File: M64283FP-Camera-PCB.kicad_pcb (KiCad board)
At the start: 2 copper layers, 21.8 x 21.4 mm, 8 parts, among them J1 JST_Connector, U1 M64283FP

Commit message: Add preview image Optimize labels
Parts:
- renumbered TADD to TP1, STRB to TP2
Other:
- board text added: "STRB"
- board text added: "TADD"
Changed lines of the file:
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@@
     (descr "SMD rectangular pad as test Point, square 1.5mm side length")
     (tags "test point SMD pad rectangle square")
-    (property "Sheetfile" "GBC Sensor breakout.kicad_sch")
+    (property "Sheetfile" "M64283FP-Camera-PCB.kicad_sch")
     (property "Sheetname" "")
     (attr exclude_from_pos_files)
-    (fp_text reference "STRB" (at 0 1.4) (layer "F.SilkS")
+    (fp_text reference "TP2" (at 0 1.4) (layer "F.SilkS") hide
       (effects (font (size 0.5 0.5) (thickness 0.1)))
     )
-    (fp_text value "TestPoint" (at 0 1.75) (layer "F.Fab")
+    (fp_text value "TestPoint" (at 0 5.461) (layer "F.Fab")
       (effects (font (size 1 1) (thickness 0.15)))
     )
@@
     (descr "Capacitor SMD 0603 (1608 Metric), square (rectangular) end terminal, IPC_7351 nominal with elongated pad for handsoldering. (Body size source: IPC-SM-782 page 76, https://www.pcb-3d.com/wordpress/wp-content/uploads/ipc-sm-782a_amendment_1_and_2.pdf), generated with kicad-footprint-generator")
     (tags "capacitor handsolder")
-    (property "Sheetfile" "GBC Sensor breakout.kicad_sch")
+    (property "Sheetfile" "M64283FP-Camera-PCB.kicad_sch")
     (property "Sheetname" "")
     (attr smd)
@@
     (descr "Inductor SMD 1210 (3225 Metric), square (rectangular) end terminal, IPC_7351 nominal with elongated pad for handsoldering. (Body size source: http://www.tortai-tech.com/upload/download/2011102023233369053.pdf), generated with kicad-footprint-generator")
     (tags "inductor handsolder")
-    (property "Sheetfile" "GBC Sensor breakout.kicad_sch")
+    (property "Sheetfile" "M64283FP-Camera-PCB.kicad_sch")
     (property "Sheetname" "")
     (attr smd)
@@
     (descr "Capacitor SMD 0603 (1608 Metric), square (rectangular) end terminal, IPC_7351 nominal with elongated pad for handsoldering. (Body size source: IPC-SM-782 page 76, https://www.pcb-3d.com/wordpress/wp-content/uploads/ipc-sm-782a_amendment_1_and_2.pdf), generated with kicad-footprint-generator")
     (tags "capacitor handsolder")
-    (property "Sheetfile" "GBC Sensor breakout.kicad_sch")
+    (property "Sheetfile" "M64283FP-Camera-PCB.kicad_sch")
     (property "Sheetname" "")
     (attr smd)
@@
   (footprint "JST Connector:JST Connector" (layer "F.Cu")
     (at 130.9 93.9 180)
-    (property "Sheetfile" "GBC Sensor breakout.kicad_sch")
+    (property "Sheetfile" "M64283FP-Camera-PCB.kicad_sch")
     (property "Sheetname" "")
     (attr smd)
@@
     (descr "SMD rectangular pad as test Point, square 1.5mm side length")
     (tags "test point SMD pad rectangle square")
-    (property "Sheetfile" "GBC Sensor breakout.kicad_sch")
+    (property "Sheetfile" "M64283FP-Camera-PCB.kicad_sch")
     (property "Sheetname" "")
     (attr exclude_from_pos_files)
-    (fp_text reference "TADD" (at 0 1.4) (layer "F.SilkS")
+    (fp_text reference "TP1" (at 0 1.4) (layer "F.SilkS") hide
       (effects (font (size 0.5 0.5) (thickness 0.1)))
     )
-    (fp_text value "TestPoint" (at 0 1.75) (layer "F.Fab")
+    (fp_text value "TestPoint" (at 0 5.461) (layer "F.Fab")
       (effects (font (size 1 1) (thickness 0.15)))
     )
@@
   (footprint "M6428xFP:M6428xFP" (layer "B.Cu")
     (at 130.9 90.05 180)
-    (property "Sheetfile" "GBC Sensor breakout.kicad_sch")
+    (property "Sheetfile" "M64283FP-Camera-PCB.kicad_sch")
     (property "Sheetname" "")
     (attr smd)
@@
   (gr_line (start 140.3 94.7) (end 140.3 92.1) (layer "Edge.Cuts") (width 0.1))
   (gr_arc (start 120 82.2) (mid 120.058579 82.058579) (end 120.2 82) (layer "Edge.Cuts") (width 0.1))
+  (gr_text "TADD" (at 132.065 99.495) (layer "F.SilkS")
+    (effects (font (size 0.5 0.5) (thickness 0.1)))
+  )
+  (gr_text "STRB" (at 135.6 99.495) (layer "F.SilkS")
+    (effects (font (size 0.5 0.5) (thickness 0.1)))
+  )
   (segment (start 136.9 90.9) (end 135.9 89.9) (width 0.25) (layer "F.Cu") (net 1))
   (segment (start 126.1625 85.4555) (end 126.1625 86.384) (width 0.25) (layer "F.Cu") (net 1))

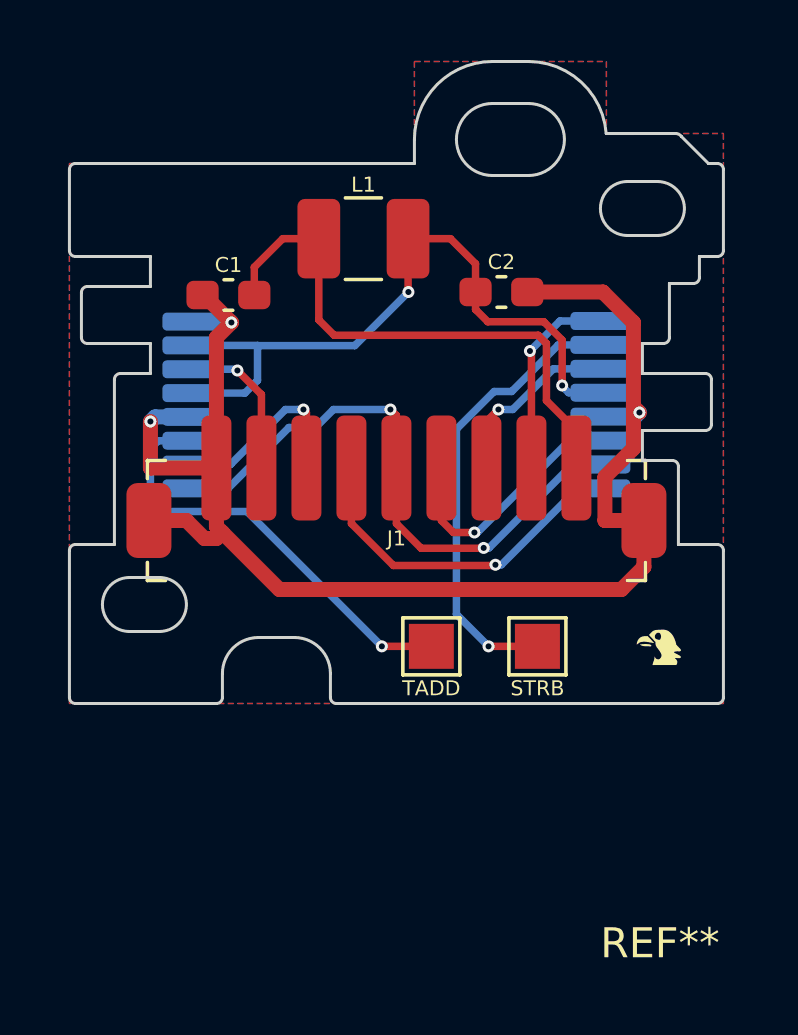
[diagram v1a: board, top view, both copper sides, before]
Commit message: Update project with new footprints and PCB shape
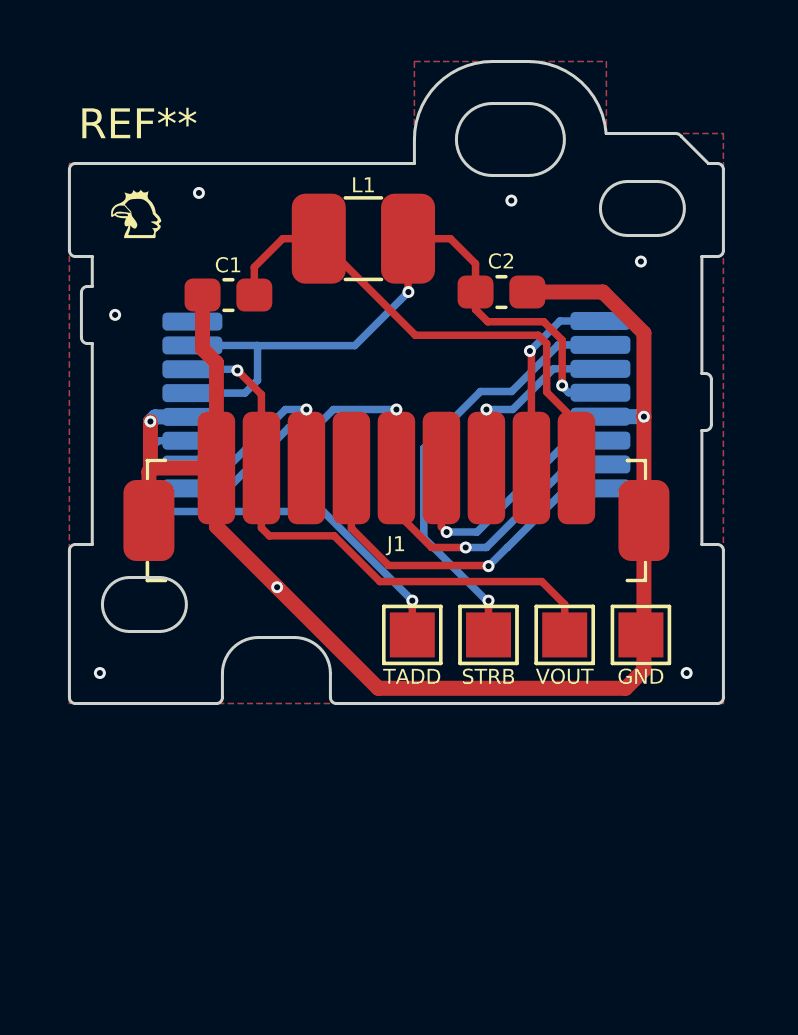
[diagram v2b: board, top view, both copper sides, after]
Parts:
- added TP3: TestPoint, TestPoint:TestPoint_Pad_1.5x1.5mm, F.Cu at (136.5, 97.7)
- added TP4: TestPoint, TestPoint:TestPoint_Pad_1.5x1.5mm, F.Cu at (139.1, 97.7)
- C1, C2: footprint Capacitor_SMD:C_0603_1608Metric_Pad1.08x0.95mm_HandSolder -> SMT (LP):0603_HandSolder (LP)
- J1: footprint JST Connector:JST Connector -> JST Connector:JST Connector (LP)
- L1: footprint Inductor_SMD:L_1210_3225Metric_Pad1.42x2.65mm_HandSolder -> SMT (LP):1210_HandSolder (LP)
- U1: footprint M6428xFP:M6428xFP -> M6428xFP:M6428xFP (LP)
- moved REF** 22.6 mm to (122.3, 83.7)
- moved TP2 1.67 mm to (134.0, 97.7)
- moved TP1 0.74 mm to (131.4, 97.7)
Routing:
- net SEN_VOUT: track 5.10 -> 19.3 mm
- net +5V: track 18.7 -> 17.1 mm
- net GND: track 48.6 -> 48.9 mm, vias 3 -> 9
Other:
- outline, holes or cut-outs redrawn
- board text added: "GND"
- board text added: "JLCJLCJLCJLC"
- board text added: "VOUT"

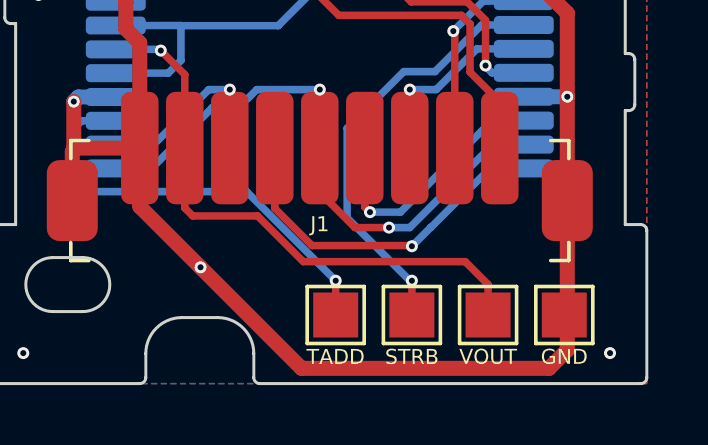
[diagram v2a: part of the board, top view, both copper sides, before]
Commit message: Add Lightproof testpoint
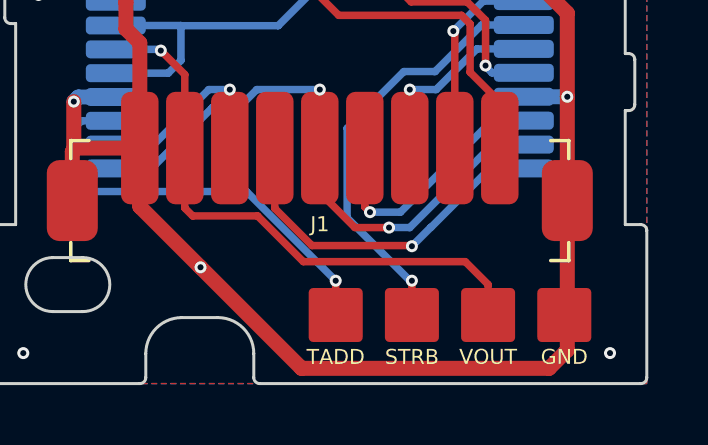
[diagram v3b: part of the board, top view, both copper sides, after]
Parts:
- TP1, TP2, TP3, TP4: footprint TestPoint:TestPoint_Pad_1.5x1.5mm -> SMT (LP):TestPoint_Pad_1.5x1.5mm (LP)
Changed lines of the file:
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@@
   (net 11 "SEN_STRB")
   (net 12 "SEN_TADD")
-  (footprint "TestPoint:TestPoint_Pad_1.5x1.5mm" (layer "F.Cu")
+  (footprint "SMT (LP):TestPoint_Pad_1.5x1.5mm (LP)" (layer "F.Cu")
     (at 139.05 97.714)
     (descr "SMD rectangular pad as test Point, square 1.5mm side length")
@@
       (effects (font (size 1 1) (thickness 0.15)))
     )
-    (fp_text value "TestPoint" (at -5.08 5.334) (layer "F.Fab")
-      (effects (font (size 1 1) (thickness 0.15)))
-    )
-    (fp_line (start 0.95 0.95) (end -0.95 0.95) (layer "F.SilkS") (width 0.12))
-    (fp_line (start 0.95 -0.95) (end 0.95 0.95) (layer "F.SilkS") (width 0.12))
-    (fp_line (start -0.95 -0.95) (end 0.95 -0.95) (layer "F.SilkS") (width 0.12))
-    (fp_line (start -0.95 0.95) (end -0.95 -0.95) (layer "F.SilkS") (width 0.12))
-    (fp_line (start -1.25 -1.25) (end -1.25 1.25) (layer "F.CrtYd") (width 0.05))
-    (fp_line (start 1.25 1.25) (end 1.25 -1.25) (layer "F.CrtYd") (width 0.05))
-    (fp_line (start 1.25 1.25) (end -1.25 1.25) (layer "F.CrtYd") (width 0.05))
-    (fp_line (start -1.25 -1.25) (end 1.25 -1.25) (layer "F.CrtYd") (width 0.05))
-    (pad "1" smd rect (at 0 0) (size 1.5 1.5) (layers "F.Cu" "F.Mask")
+    (fp_text value "TestPoint" (at -3.683 5.08) (layer "F.Fab") hide
+      (effects (font (size 1 1) (thickness 0.15)))
+    )
+    (fp_text user "${REFERENCE}" (at 0 -1.65) (layer "F.Fab") hide
+      (effects (font (size 1 1) (thickness 0.15)))
+    )
+    (pad "" smd roundrect (at 0 0) (size 1.5 1.5) (layers "F.Paste" "F.Mask") (roundrect_rratio 0.1))
+    (pad "1" smd roundrect (at 0 0) (size 1.8 1.8) (layers "F.Cu" "F.Paste") (roundrect_rratio 0.08333333333)
       (net 2 "GND") (pinfunction "1") (pintype "passive"))
   )
-  (footprint "TestPoint:TestPoint_Pad_1.5x1.5mm" (layer "F.Cu")
+  (footprint "SMT (LP):TestPoint_Pad_1.5x1.5mm (LP)" (layer "F.Cu")
     (at 133.97 97.714)
     (descr "SMD rectangular pad as test Point, square 1.5mm side length")
@@
     (property "Sheetname" "")
     (attr exclude_from_pos_files)
-    (fp_text reference "TP2" (at 0 1.4) (layer "F.SilkS") hide
-      (effects (font (size 0.5 0.5) (thickness 0.1)))
-    )
-    (fp_text value "TestPoint" (at 0 5.334) (layer "F.Fab")
-      (effects (font (size 1 1) (thickness 0.15)))
-    )
-    (fp_line (start 0.95 0.95) (end -0.95 0.95) (layer "F.SilkS") (width 0.12))
-    (fp_line (start -0.95 0.95) (end -0.95 -0.95) (layer "F.SilkS") (width 0.12))
-    (fp_line (start -0.95 -0.95) (end 0.95 -0.95) (layer "F.SilkS") (width 0.12))
-    (fp_line (start 0.95 -0.95) (end 0.95 0.95) (layer "F.SilkS") (width 0.12))
-    (fp_line (start 1.25 1.25) (end -1.25 1.25) (layer "F.CrtYd") (width 0.05))
-    (fp_line (start 1.25 1.25) (end 1.25 -1.25) (layer "F.CrtYd") (width 0.05))
-    (fp_line (start -1.25 -1.25) (end -1.25 1.25) (layer "F.CrtYd") (width 0.05))
-    (fp_line (start -1.25 -1.25) (end 1.25 -1.25) (layer "F.CrtYd") (width 0.05))
-    (pad "1" smd rect (at 0 0) (size 1.5 1.5) (layers "F.Cu" "F.Mask")
+    (fp_text reference "TP2" (at 0 -1.648) (layer "F.SilkS") hide
+      (effects (font (size 1 1) (thickness 0.15)))
+    )
+    (fp_text value "TestPoint" (at 1.397 5.08) (layer "F.Fab") hide
+      (effects (font (size 1 1) (thickness 0.15)))
+    )
+    (fp_text user "${REFERENCE}" (at 0 -1.65) (layer "F.Fab") hide
+      (effects (font (size 1 1) (thickness 0.15)))
+    )
+    (pad "" smd roundrect (at 0 0) (size 1.5 1.5) (layers "F.Paste" "F.Mask") (roundrect_rratio 0.1))
+    (pad "1" smd roundrect (at 0 0) (size 1.8 1.8) (layers "F.Cu" "F.Paste") (roundrect_rratio 0.08333333333)
       (net 11 "SEN_STRB") (pinfunction "1") (pintype "passive"))
   )
@@
     )
   )
-  (footprint "TestPoint:TestPoint_Pad_1.5x1.5mm" (layer "F.Cu")
+  (footprint "SMT (LP):TestPoint_Pad_1.5x1.5mm (LP)" (layer "F.Cu")
     (at 136.51 97.714)
     (descr "SMD rectangular pad as test Point, square 1.5mm side length")
@@
       (effects (font (size 1 1) (thickness 0.15)))
     )
-    (fp_text value "TestPoint" (at -2.54 5.334) (layer "F.Fab")
-      (effects (font (size 1 1) (thickness 0.15)))
-    )
-    (fp_line (start -0.95 0.95) (end -0.95 -0.95) (layer "F.SilkS") (width 0.12))
-    (fp_line (start 0.95 0.95) (end -0.95 0.95) (layer "F.SilkS") (width 0.12))
-    (fp_line (start 0.95 -0.95) (end 0.95 0.95) (layer "F.SilkS") (width 0.12))
-    (fp_line (start -0.95 -0.95) (end 0.95 -0.95) (layer "F.SilkS") (width 0.12))
-    (fp_line (start -1.25 -1.25) (end -1.25 1.25) (layer "F.CrtYd") (width 0.05))
-    (fp_line (start 1.25 1.25) (end -1.25 1.25) (layer "F.CrtYd") (width 0.05))
-    (fp_line (start -1.25 -1.25) (end 1.25 -1.25) (layer "F.CrtYd") (width 0.05))
-    (fp_line (start 1.25 1.25) (end 1.25 -1.25) (layer "F.CrtYd") (width 0.05))
-    (pad "1" smd rect (at 0 0) (size 1.5 1.5) (layers "F.Cu" "F.Mask")
+    (fp_text value "TestPoint" (at -1.143 5.08) (layer "F.Fab") hide
+      (effects (font (size 1 1) (thickness 0.15)))
+    )
+    (fp_text user "${REFERENCE}" (at 0 -1.65) (layer "F.Fab") hide
+      (effects (font (size 1 1) (thickness 0.15)))
+    )
+    (pad "" smd roundrect (at 0 0) (size 1.5 1.5) (layers "F.Paste" "F.Mask") (roundrect_rratio 0.1))
+    (pad "1" smd roundrect (at 0 0) (size 1.8 1.8) (layers "F.Cu" "F.Paste") (roundrect_rratio 0.08333333333)
       (net 10 "SEN_VOUT") (pinfunction "1") (pintype "passive"))
   )
@@
       ) (layer "F.Mask") (width 0) (fill solid))
   )
-  (footprint "TestPoint:TestPoint_Pad_1.5x1.5mm" (layer "F.Cu")
+  (footprint "SMT (LP):TestPoint_Pad_1.5x1.5mm (LP)" (layer "F.Cu")
     (at 131.43 97.714)
     (descr "SMD rectangular pad as test Point, square 1.5mm side length")
@@
     (property "Sheetname" "")
     (attr exclude_from_pos_files)
-    (fp_text reference "TP1" (at 0 1.4) (layer "F.SilkS") hide
-      (effects (font (size 0.5 0.5) (thickness 0.1)))
-    )
-    (fp_text value "TestPoint" (at 2.54 5.334) (layer "F.Fab")
-      (effects (font (size 1 1) (thickness 0.15)))
-    )
-    (fp_line (start 0.95 -0.95) (end 0.95 0.95) (layer "F.SilkS") (width 0.12))
-    (fp_line (start 0.95 0.95) (end -0.95 0.95) (layer "F.SilkS") (width 0.12))
-    (fp_line (start -0.95 -0.95) (end 0.95 -0.95) (layer "F.SilkS") (width 0.12))
-    (fp_line (start -0.95 0.95) (end -0.95 -0.95) (layer "F.SilkS") (width 0.12))
-    (fp_line (start -1.25 -1.25) (end -1.25 1.25) (layer "F.CrtYd") (width 0.05))
-    (fp_line (start 1.25 1.25) (end -1.25 1.25) (layer "F.CrtYd") (width 0.05))
-    (fp_line (start -1.25 -1.25) (end 1.25 -1.25) (layer "F.CrtYd") (width 0.05))
-    (fp_line (start 1.25 1.25) (end 1.25 -1.25) (layer "F.CrtYd") (width 0.05))
-    (pad "1" smd rect (at 0 0) (size 1.5 1.5) (layers "F.Cu" "F.Mask")
+    (fp_text reference "TP1" (at 0 -1.648) (layer "F.SilkS") hide
+      (effects (font (size 1 1) (thickness 0.15)))
+    )
+    (fp_text value "TestPoint" (at 3.937 5.08) (layer "F.Fab") hide
+      (effects (font (size 1 1) (thickness 0.15)))
+    )
+    (fp_text user "${REFERENCE}" (at 0 -1.65) (layer "F.Fab") hide
+      (effects (font (size 1 1) (thickness 0.15)))
+    )
+    (pad "" smd roundrect (at 0 0) (size 1.5 1.5) (layers "F.Paste" "F.Mask") (roundrect_rratio 0.1))
+    (pad "1" smd roundrect (at 0 0) (size 1.8 1.8) (layers "F.Cu" "F.Paste") (roundrect_rratio 0.08333333333)
       (net 12 "SEN_TADD") (pinfunction "1") (pintype "passive"))
   )
